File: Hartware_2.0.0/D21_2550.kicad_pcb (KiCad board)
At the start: 2 copper layers, 80 x 55 mm, 54 parts, among them P1 CONN_01X05, P2 CONN_01X02, P3 CONN_01X02, P4 ISCP, Q1 FZT493TA, Q2 FZT493TA, Q3 FZT493TA, SW1 SW_PUSH, SW2 SW_PUSH, SW3 SW_PUSH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

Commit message: modificacion de cartas
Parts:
- removed R27: 100, Resistor_SMD:R_0805_2012Metric_Pad1.15x1.50mm_HandSolder
- added C1: 4,7uF, Capacitor_THT:CP_Radial_D8.0mm_P3.50mm, F.Cu at (136.0, 70.0)
- added C10: CP1, Capacitor_SMD:CP_Elec_3x5.3, F.Cu at (146.0, 71.0)
- added C11: 4,7uF, Capacitor_THT:CP_Radial_D8.0mm_P3.50mm, F.Cu at (143.0, 77.0)
- added C2: 33pf, Capacitor_SMD:C_0805_2012Metric_Pad1.15x1.50mm_HandSolder, F.Cu at (89.0, 44.0)
- added C3: 33pf, Capacitor_SMD:C_0805_2012Metric_Pad1.15x1.50mm_HandSolder, F.Cu at (89.0, 46.0)
- added C8: 1nF, Capacitor_SMD:C_0805_2012Metric_Pad1.15x1.50mm_HandSolder, F.Cu at (154.5, 58.0)
- added C9: CP1, Capacitor_SMD:CP_Elec_3x5.3, F.Cu at (152.0, 71.0)
- added D7: 1N4007, Diode_SMD:D_SOD-123, B.Cu at (83.5, 78.8)
- added L1: SDR0503-472JL, Devices_MSS:SDR0503-XXX, F.Cu at (142.0, 45.1)
- added L2: 74479776247, Inductor_SMD:L_0805_2012Metric_Pad1.15x1.50mm_HandSolder, F.Cu at (153.0, 52.0)
- added R1: 300k, Resistor_SMD:R_1206_3216Metric_Pad1.24x1.80mm_HandSolder, F.Cu at (148.4, 46.0)
- added RV1: B72214S0351K101, Capacitor_THT:C_Disc_D4.3mm_W1.9mm_P5.00mm, F.Cu at (147.0, 43.0)
- added TH1: Thermistor_NTC, Resistor_SMD:R_0805_2012Metric_Pad1.15x1.50mm_HandSolder, F.Cu at (152.5, 49.0)
- added U8: PBO-3-S5, Devices_MSS:PBO-3-S5, B.Cu at (157.0, 60.5)
- P1: value CONN_01X05 -> POWER I/O
- U2, U3, U4: footprint Package_SOIC:SO-6_4.4x3.6mm_P1.27mm -> Devices_MSS:MOC306X
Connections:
- P1 pad 1: (no net) -> Vac
- U5 pad 2: Net-(U2-Pad4) -> CO
- U5 pad 3: CO -> Net-(U2-Pad4)
- U6 pad 2: Net-(U3-Pad4) -> VE
- U6 pad 3: VE -> Net-(U3-Pad4)
- U7 pad 2: Net-(U4-Pad4) -> RE
- U7 pad 3: RE -> Net-(U4-Pad4)
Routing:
- net Nac: track 44.0 -> 0.00 mm, vias 2 -> 0
- net RE: track 17.6 -> 0.00 mm
- net CO: track 16.1 -> 0.00 mm, vias 1 -> 0
- net Net-(U2-Pad4): track 12.4 -> 0.00 mm, vias 1 -> 0
- net Net-(U3-Pad4): track 4.84 -> 0.00 mm, vias 1 -> 0
- net Net-(R8-Pad2): track 3.19 -> 0.57 mm
- net /Cerebro/Salida de potencia/Ventilador: track 69.3 -> 67.8 mm
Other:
- board size 80 x 55 mm -> 80 x 60 mm

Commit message: a medio hacer
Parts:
- added C12: 0.1uF, Capacitor_SMD:C_1206_3216Metric_Pad1.24x1.80mm_HandSolder, F.Cu at (168.2, 127.5)
- C10: value CP1 -> 68uF; footprint Capacitor_SMD:CP_Elec_3x5.3 -> Capacitor_SMD:CP_Elec_6.3x7.7
- C2, C3, R2: moved to B.Cu
- C4, C5, C6: footprint Capacitor_THT:C_Disc_D9.0mm_W2.5mm_P5.00mm -> Capacitor_SMD:C_2225_5664Metric_Pad1.78x6.70mm_HandSolder
- C9: value CP1 -> 270uF; footprint Capacitor_SMD:CP_Elec_3x5.3 -> Capacitor_SMD:CP_Elec_6.3x7.7
- D10: value D_R -> LED; footprint LED_SMD:LED_PLCC-2 -> LED_SMD:LED_0603_1608Metric_Pad0.67x1.00mm_HandSolder
- D6: value 1N4007 -> 1N4148X-TP; footprint Diode_SMD:D_SOD-123 -> Diode_SMD:D_SOD-523; moved to B.Cu
- D7: value 1N4007 -> 1N4148X-TP; footprint Diode_SMD:D_SOD-123 -> Diode_SMD:D_SOD-523
- D8: value D_C -> LED; footprint LED_SMD:LED_PLCC-2 -> LED_SMD:LED_0603_1608Metric_Pad0.67x1.00mm_HandSolder
- D9: value D_V -> LED; footprint LED_SMD:LED_PLCC-2 -> LED_SMD:LED_0603_1608Metric_Pad0.67x1.00mm_HandSolder
- P1: footprint Connector_Molex:Molex_Micro-Fit_3.0_43650-0515_1x05_P3.00mm_Vertical -> TerminalBlock:TerminalBlock_bornier-5_P5.08mm
- R10, R11, R9: footprint Resistor_THT:R_Axial_DIN0309_L9.0mm_D3.2mm_P12.70mm_Horizontal -> Resistor_SMD:R_1210_3225Metric_Pad1.24x2.70mm_HandSolder
- R3, R4, R5, R6, R7, R8, U2, U3, U4: moved to F.Cu
- U5, U6, U7: footprint Package_TO_SOT_SMD:SOT-223 -> Devices_MSS:SOT-223-Z01
- Y1: value 4MHZ -> 20MHZ; footprint Crystal:Crystal_SMD_5032-2Pin_5.0x3.2mm_HandSoldering -> Devices_MSS:Crystal_SMD_ABLS_HC49-SD
- moved R5 184.2 mm to (182.3, 236.4), turned to 0 degrees
- moved R3 178.8 mm to (198.2, 233.4), turned to 0 degrees
- moved R8 178.5 mm to (178.0, 236.4), turned to 0 degrees
- moved R4 176.5 mm to (212.1, 216.8), turned to 0 degrees
- moved U5 175.5 mm to (240.6, 186.7), turned to 0 degrees
- moved R7 170.8 mm to (169.6, 236.5), turned to 0 degrees
- moved C4 163.8 mm to (205.9, 224.5)
- moved C5 162.6 mm to (205.9, 213.4)
- moved C6 161.8 mm to (191.9, 235.9)
- moved R10 161.1 mm to (164.7, 237.2)
- moved R6 160.0 mm to (212.1, 210.9), turned to 0 degrees
- moved R9 154.6 mm to (159.1, 237.2)
- moved U6 135.8 mm to (166.6, 198.3)
- moved R11 130.8 mm to (211.6, 195.2)
- moved U7 128.3 mm to (196.1, 185.2)
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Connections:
- net Net-(C9-Pad1) renamed /Fuente/VO
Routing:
- net VDD: track 22.8 -> 164.1 mm, vias 0 -> 3
- net /Cerebro/Salida de potencia/Compresor: track 73.7 -> 0.00 mm, vias 2 -> 0
- net /Cerebro/Salida de potencia/Ventilador: track 67.8 -> 0.00 mm, vias 2 -> 0
- net /Cerebro/Salida de potencia/Resistencia: track 62.5 -> 0.00 mm, vias 2 -> 0
- net /Cerebro/Botones/+: track 16.7 -> 58.9 mm
- net GND: track 176.0 -> 212.5 mm, vias 8 -> 3
- net /Cerebro/Botones/-: track 20.4 -> 47.6 mm
- net VDDP: track 0.00 -> 24.6 mm, vias 0 -> 1
- net /Fuente/VO: track 0.00 -> 24.4 mm
- net /Cerebro/7 SEGMENTOS/F: track 27.6 -> 51.8 mm
- net /Cerebro/7 SEGMENTOS/E1: track 19.0 -> 43.2 mm
- net /Cerebro/7 SEGMENTOS/A: track 26.1 -> 47.8 mm, vias 1 -> 0
- net /Cerebro/7 SEGMENTOS/B: track 29.3 -> 50.0 mm, vias 1 -> 0
- net Net-(C1-Pad2): track 0.00 -> 18.8 mm
- net VPP: track 4.49 -> 22.5 mm
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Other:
- board size 80 x 60 mm -> 105 x 60 mm

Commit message: final placa v2
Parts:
- C12: value 0.1uF -> 100nF
- C4, C5, C6: value 100nf -> 100nF; footprint Capacitor_SMD:C_2225_5664Metric_Pad1.78x6.70mm_HandSolder -> Capacitor_SMD:C_1206_3216Metric_Pad1.24x1.80mm_HandSolder; moved to B.Cu
- R10, R11, R9, U5, U6, U7: moved to B.Cu
- SW1, SW2, SW3, SW4: value SW_PUSH -> TL3305AF260QG; footprint Button_Switch_SMD:SW_SPST_EVPBF -> Devices_MSS:tl3305
- moved R7 154.1 mm to (172.8, 82.5), turned to 180 degrees
- moved R8 154.0 mm to (182.5, 82.5), turned to 180 degrees
- moved R3 140.5 mm to (166.6, 96.5)
- moved R10 140.1 mm to (176.6, 97.6), turned to 270 degrees
- moved R5 139.9 mm to (185.2, 96.5)
- moved R9 139.4 mm to (165.7, 98.0), turned to 270 degrees
- moved R6 137.3 mm to (163.3, 82.5), turned to 180 degrees
- moved C6 132.3 mm to (183.4, 104.0), turned to 270 degrees
- moved C4 127.1 mm to (165.7, 104.0), turned to 270 degrees
- moved R4 125.8 mm to (175.6, 96.5)
- moved U5 123.2 mm to (165.0, 89.5), turned to 270 degrees
- moved C5 113.3 mm to (176.6, 104.0), turned to 270 degrees
- moved U6 109.1 mm to (174.2, 89.5), turned to 270 degrees
- moved R11 101.5 mm to (183.4, 97.7), turned to 270 degrees
- moved U7 96.5 mm to (183.6, 89.5), turned to 270 degrees
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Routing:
- net GND: track 212.5 -> 314.9 mm, vias 3 -> 8
- net Nac: track 4.82 -> 81.9 mm
- net /Cerebro/Salida de potencia/Resistencia: track 0.00 -> 76.9 mm, vias 0 -> 1
- net /Cerebro/Salida de potencia/Ventilador: track 0.00 -> 68.4 mm, vias 0 -> 1
- net VE: track 0.00 -> 52.5 mm, vias 0 -> 3
- net /Cerebro/Salida de potencia/Compresor: track 0.00 -> 52.4 mm, vias 0 -> 1
- net RE: track 0.00 -> 51.0 mm, vias 0 -> 1
- net CO: track 0.00 -> 49.0 mm, vias 0 -> 2
- net Vac: track 4.00 -> 49.5 mm
- net /Cerebro/Botones/S: track 76.7 -> 39.2 mm
- net /Cerebro/Acond NTC/T_A: track 0.00 -> 33.4 mm, vias 0 -> 1
- net /Cerebro/Acond NTC/T_R: track 0.00 -> 29.3 mm, vias 0 -> 1
- net /Cerebro/Botones/P: track 57.6 -> 38.1 mm
- net /Cerebro/Botones/+: track 58.9 -> 42.1 mm
- net VDD: track 164.1 -> 147.3 mm, vias 3 -> 5
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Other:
- board size 105 x 60 mm -> 95 x 55 mm

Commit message: termino parcial de la version 2
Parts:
- added REF**: MountingHole_3.2mm_M3_DIN965_Pad, MountingHole:MountingHole_3.2mm_M3_DIN965_Pad, F.Cu at (99.0, 131.0)
- added REF**: MountingHole_3.2mm_M3_DIN965_Pad, MountingHole:MountingHole_3.2mm_M3_DIN965_Pad, F.Cu at (169.0, 124.0)
- P2: value CONN_01X02 -> TA
- P3: value CONN_01X02 -> TR
- SW1, SW2, SW3, SW4: value TL3305AF260QG -> TL3301AF160QG; footprint Devices_MSS:tl3305 -> Devices_MSS:TL3301AF160QG
- moved R22 12.2 mm to (127.0, 84.0), turned to 270 degrees
- moved R23 7.78 mm to (130.0, 84.0)
- moved SW3 7.09 mm to (119.2, 89.0)
- moved SW4 7.07 mm to (119.0, 97.0), turned to 180 degrees
- moved SW1 1.41 mm to (103.0, 89.0), turned to 0 degrees
- moved SW2 1.41 mm to (103.0, 97.0)
- moved R21 0.44 mm to (110.4, 96.0), turned to 270 degrees
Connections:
- P1 pad 2: RE -> CO
- P1 pad 4: CO -> RE
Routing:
- net GND: track 314.9 -> 362.0 mm, vias 8 -> 7
- net VDD: track 147.3 -> 161.0 mm, vias 5 -> 6
- net RE: track 51.0 -> 40.0 mm, vias 1 -> 2
- net /Cerebro/Botones/P: track 38.1 -> 48.9 mm
- net /Cerebro/Botones/S: track 39.2 -> 47.8 mm
- net Vac: track 49.5 -> 57.9 mm
- net CO: track 49.0 -> 55.9 mm
- net /Cerebro/Botones/+: track 42.1 -> 45.4 mm
- net /Cerebro/Botones/-: track 36.5 -> 34.4 mm
- net Nac: track 81.9 -> 83.6 mm
- net /Cerebro/Salida de potencia/Compresor: track 52.4 -> 53.7 mm
- net Net-(L1-Pad2): track 9.51 -> 10.1 mm
- net VE: track 52.5 -> 52.1 mm, vias 3 -> 2

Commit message: agregando BOM
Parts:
- C7: footprint Capacitor_SMD:CP_Elec_3x5.3 -> Capacitor_SMD:CP_Elec_4x5.3
- moved C7 0.32 mm to (107.2, 127.1)
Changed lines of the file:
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@@
   )
   (setup
-    (last_trace_width 0.5)
+    (last_trace_width 0.25)
     (user_trace_width 0.2)
     (user_trace_width 0.3)
@@
     )
   )
-  (module Capacitor_SMD:CP_Elec_3x5.3 (layer B.Cu)
-    (at 106.9 127.13)
-    (descr "SMT capacitor, aluminium electrolytic, 3x5.3")
-    (attr smd)
-    (fp_text reference C7 (at 0 -2.9) (layer B.SilkS)
-      (effects (font (size 1 1) (thickness 0.15)) (justify mirror))
-    )
-    (fp_text value 10uf (at -0.03 2.9) (layer B.Fab)
-      (effects (font (size 1 1) (thickness 0.15)) (justify mirror))
-    )
-    (fp_circle (center 0 0) (end 0.3 -1.5) (layer B.Fab) (width 0.1))
-    (fp_text user + (at -0.94 0.08) (layer B.Fab)
-      (effects (font (size 1 1) (thickness 0.15)) (justify mirror))
-    )
-    (fp_text user + (at -2.22 -1.4) (layer B.SilkS)
-      (effects (font (size 1 1) (thickness 0.15)) (justify mirror))
-    )
-    (fp_text user %R (at 0 -2.9) (layer B.Fab)
-      (effects (font (size 1 1) (thickness 0.15)) (justify mirror))
-    )
-    (fp_line (start -1.56 0.75) (end -1.56 -0.77) (layer B.Fab) (width 0.1))
-    (fp_line (start -0.75 1.56) (end -1.56 0.75) (layer B.Fab) (width 0.1))
-    (fp_line (start -0.76 -1.57) (end -1.56 -0.77) (layer B.Fab) (width 0.1))
-    (fp_line (start 1.57 -1.57) (end 1.57 1.56) (layer B.Fab) (width 0.1))
-    (fp_line (start 1.56 -1.57) (end -0.76 -1.57) (layer B.Fab) (width 0.1))
-    (fp_line (start 1.57 1.56) (end -0.75 1.56) (layer B.Fab) (width 0.1))
-    (fp_line (start -0.83 -1.73) (end -1.44 -1.12) (layer B.SilkS) (width 0.12))
-    (fp_line (start 1.73 -1.73) (end 1.73 -1.12) (layer B.SilkS) (width 0.12))
-    (fp_line (start -0.81 1.71) (end -1.41 1.12) (layer B.SilkS) (width 0.12))
-    (fp_line (start 1.73 1.71) (end 1.73 1.12) (layer B.SilkS) (width 0.12))
-    (fp_line (start -0.83 -1.73) (end 1.71 -1.73) (layer B.SilkS) (width 0.12))
-    (fp_line (start 1.73 1.71) (end -0.81 1.71) (layer B.SilkS) (width 0.12))
-    (fp_line (start -2.85 1.82) (end 2.85 1.82) (layer B.CrtYd) (width 0.05))
-    (fp_line (start -2.85 1.82) (end -2.85 -1.82) (layer B.CrtYd) (width 0.05))
-    (fp_line (start 2.85 -1.82) (end 2.85 1.82) (layer B.CrtYd) (width 0.05))
-    (fp_line (start 2.85 -1.82) (end -2.85 -1.82) (layer B.CrtYd) (width 0.05))
-    (pad 2 smd rect (at 1.5 0) (size 2.2 1.6) (layers B.Cu B.Paste B.Mask)
-      (net 1 GND))
-    (pad 1 smd rect (at -1.5 0) (size 2.2 1.6) (layers B.Cu B.Paste B.Mask)
-      (net 47 "Net-(C7-Pad1)"))
-    (model ${KISYS3DMOD}/Capacitor_SMD.3dshapes/CP_Elec_3x5.3.wrl
-      (at (xyz 0 0 0))
-      (scale (xyz 1 1 1))
-      (rotate (xyz 0 0 0))
-    )
-  )
   (module Capacitor_SMD:C_0805_2012Metric_Pad1.15x1.50mm_HandSolder (layer F.Cu)
     (at 160.2 121.0575 270)
@@
       (scale (xyz 1 1 1))
       (rotate (xyz 0 0 0))
+    )
+  )
+  (module Capacitor_SMD:CP_Elec_4x5.3 (layer B.Cu)
+    (at 107.22 127.14)
+    (descr "SMT capacitor, aluminium electrolytic, 4x5.3")
+    (attr smd)
+    (fp_text reference C7 (at 0 -3.54) (layer B.SilkS)
+      (effects (font (size 1 1) (thickness 0.15)) (justify mirror))
+    )
+    (fp_text value 10uf (at 0 3.54) (layer B.Fab)
+      (effects (font (size 1 1) (thickness 0.15)) (justify mirror))
+    )
+    (fp_circle (center 0 0) (end 0 -2.1) (layer B.Fab) (width 0.1))
+    (fp_text user + (at -1.21 0.08) (layer B.Fab)
+      (effects (font (size 1 1) (thickness 0.15)) (justify mirror))
+    )
+    (fp_text user + (at -2.77 -2.01) (layer B.SilkS)
+      (effects (font (size 1 1) (thickness 0.15)) (justify mirror))
+    )
+    (fp_text user %R (at 0 -3.54) (layer B.Fab)
+      (effects (font (size 1 1) (thickness 0.15)) (justify mirror))
+    )
+    (fp_line (start 2.13 -2.13) (end 2.13 2.13) (layer B.Fab) (width 0.1))
+    (fp_line (start -1.46 -2.13) (end 2.13 -2.13) (layer B.Fab) (width 0.1))
+    (fp_line (start -2.13 -1.46) (end -1.46 -2.13) (layer B.Fab) (width 0.1))
+    (fp_line (start -2.13 1.46) (end -2.13 -1.46) (layer B.Fab) (width 0.1))
+    (fp_line (start -1.46 2.13) (end -2.13 1.46) (layer B.Fab) (width 0.1))
+    (fp_line (start 2.13 2.13) (end -1.46 2.13) (layer B.Fab) (width 0.1))
+    (fp_line (start -2.29 1.52) (end -2.29 1.12) (layer B.SilkS) (width 0.12))
+    (fp_line (start 2.29 2.29) (end 2.29 1.12) (layer B.SilkS) (width 0.12))
+    (fp_line (start 2.29 -2.29) (end 2.29 -1.12) (layer B.SilkS) (width 0.12))
+    (fp_line (start -2.29 -1.52) (end -2.29 -1.12) (layer B.SilkS) (width 0.12))
+    (fp_line (start -1.52 -2.29) (end 2.29 -2.29) (layer B.SilkS) (width 0.12))
+    (fp_line (start -1.52 -2.29) (end -2.29 -1.52) (layer B.SilkS) (width 0.12))
+    (fp_line (start -1.52 2.29) (end 2.29 2.29) (layer B.SilkS) (width 0.12))
+    (fp_line (start -1.52 2.29) (end -2.29 1.52) (layer B.SilkS) (width 0.12))
+    (fp_line (start -3.35 2.39) (end 3.35 2.39) (layer B.CrtYd) (width 0.05))
+    (fp_line (start -3.35 2.39) (end -3.35 -2.38) (layer B.CrtYd) (width 0.05))
+    (fp_line (start 3.35 -2.38) (end 3.35 2.39) (layer B.CrtYd) (width 0.05))
+    (fp_line (start 3.35 -2.38) (end -3.35 -2.38) (layer B.CrtYd) (width 0.05))
+    (pad 1 smd rect (at -1.8 0 180) (size 2.6 1.6) (layers B.Cu B.Paste B.Mask)
+      (net 47 "Net-(C7-Pad1)"))
+    (pad 2 smd rect (at 1.8 0 180) (size 2.6 1.6) (layers B.Cu B.Paste B.Mask)
+      (net 1 GND))
+    (model ${KISYS3DMOD}/Capacitor_SMD.3dshapes/CP_Elec_4x5.3.wrl
+      (at (xyz 0 0 0))
+      (scale (xyz 1 1 1))
+      (rotate (xyz 0 0 0))

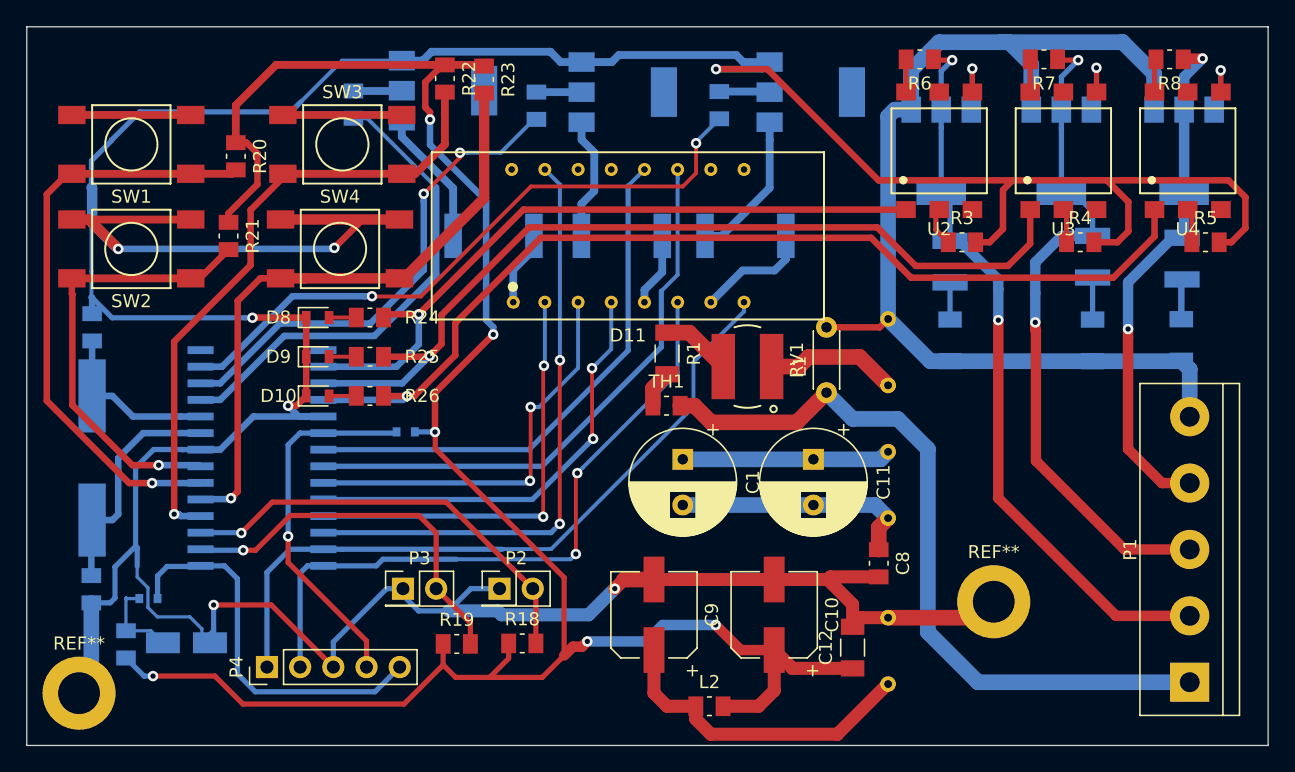
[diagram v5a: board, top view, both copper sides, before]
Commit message: creando archivo step
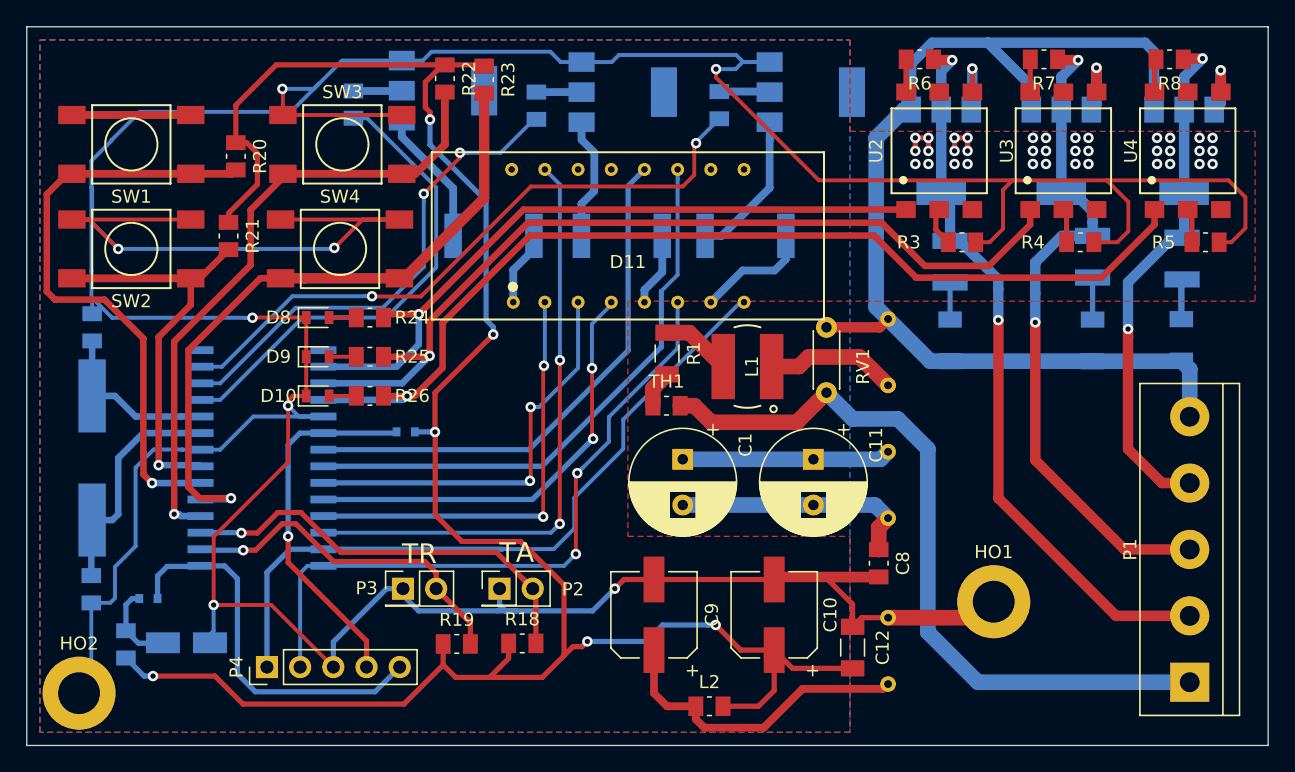
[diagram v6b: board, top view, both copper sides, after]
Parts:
- renumbered REF** to HO1, REF** to HO2
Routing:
- net GND: track 362.0 -> 386.1 mm, vias 7 -> 44
- net /Cerebro/Botones/S: track 47.8 -> 51.9 mm
- net /Cerebro/Botones/-: track 34.4 -> 31.5 mm
- net VDD: track 161.0 -> 163.6 mm
- net /Cerebro/Acond NTC/T_R: track 29.3 -> 27.0 mm
- net Nac: track 83.6 -> 85.1 mm
- net /Cerebro/Botones/+: track 45.4 -> 46.6 mm
- net /Cerebro/Acond NTC/T_A: track 33.4 -> 34.0 mm
- added copper zone on B.Cu, net GND
- added copper zone on F.Cu, net GND
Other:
- board text added: "TA"
- board text added: "TR"
